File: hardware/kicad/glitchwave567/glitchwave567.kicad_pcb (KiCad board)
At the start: 2 copper layers, 0 parts

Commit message: hardware: LAYOUT phase 1 - both boards placed via pcbnew API (296+22 footprints, nets bound)
pcbgen.py: netlist-driven board authoring (pcbnew python 7.0.11) - footprint
instantiation with per-pad net binding, corner-notched outline, spiral
auto-placement of passives near net-neighbor anchors (pad-extent collision),
GND zones both layers staged. Wall jacks auto-oriented; audit confirms zero
pads outside outline. Audio chain right-to-left (IN->dirt->567->SVF->OUT),
buck top-center, Pico+digital bottom, ctrl board pots 3+3 grid at drill
positions, header at identical enclosure XY on both boards (stack mates).
Routing (custom grid A*) next.

Co-Authored-By: Claude Fable 5 <noreply@anthropic.com>
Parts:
- added C1: 220n, C_0603_1608Metric, F.Cu at (126.4, 42.0)
- added C100: 220u/35V, CP_Elec_8x10, F.Cu at (70.8, 25.0)
- added C101: 100n, C_0603_1608Metric, F.Cu at (70.0, 28.2)
- added C102: 1u, C_0603_1608Metric, F.Cu at (70.0, 21.8)
- added C103: 1u, C_0603_1608Metric, F.Cu at (73.8, 27.9)
- added C104: 10u/50V X7R, C_1206_3216Metric, F.Cu at (72.0, 31.1)
- added C105: 3n3, C_0603_1608Metric, F.Cu at (73.8, 22.1)
- added C106: 100n, C_0603_1608Metric, F.Cu at (88.0, 20.0)
- added C107: 100n, C_0603_1608Metric, F.Cu at (66.3, 29.2)
- added C108: 22u, C_0805_2012Metric, F.Cu at (64.8, 21.2)
- added C109: 47u, CP_Elec_6.3x5.4, F.Cu at (53.8, 36.3)
- added C110: 47u, CP_Elec_6.3x5.4, F.Cu at (68.4, 18.0)
- added C111: 100n, C_0603_1608Metric, F.Cu at (63.0, 26.6)
- added C120: 1n, C_0603_1608Metric, F.Cu at (48.7, 109.5)
- added C121: 100n, C_0603_1608Metric, F.Cu at (75.7, 19.3)
- added C122: 100n, C_0603_1608Metric, F.Cu at (76.6, 30.8)
- added C123: 100n, C_0603_1608Metric, F.Cu at (97.6, 106.8)
- added C124: 100n, C_0603_1608Metric, F.Cu at (93.2, 106.8)
- added C2: 4.7u, CP_Elec_4x5.4, F.Cu at (75.0, 34.1)
- added C20: 100n, C_0603_1608Metric, F.Cu at (122.0, 48.1)
- added C21: 100n, C_0603_1608Metric, F.Cu at (122.4, 50.5)
- added C22: 100n, C_0603_1608Metric, F.Cu at (117.3, 47.8)
- added C23: 100n, C_0603_1608Metric, F.Cu at (117.7, 50.2)
- added C3: 220n, C_0603_1608Metric, F.Cu at (114.0, 44.4)
- added C30: 100n, C_0603_1608Metric, F.Cu at (128.0, 79.2)
- added C31: 100n, C_0603_1608Metric, F.Cu at (128.0, 72.8)
- added C32: 3.9n, C_0603_1608Metric, F.Cu at (62.1, 28.8)
- added C33: 100n, C_0603_1608Metric, F.Cu at (61.2, 24.2)
- added C34: 100n, C_0603_1608Metric, F.Cu at (78.2, 21.9)
- added C35: 100n, C_0603_1608Metric, F.Cu at (60.9, 21.9)
- added C40: 100n, C_0603_1608Metric, F.Cu at (69.2, 15.4)
- added C41: DNP-LFIL, C_0603_1608Metric, F.Cu at (97.0, 54.0)
- added C42: DNP-OFIL, C_0603_1608Metric, F.Cu at (97.0, 46.0)
- added C43: 220p, C_0603_1608Metric, F.Cu at (73.5, 15.2)
- added C44: 1u, C_0603_1608Metric, F.Cu at (77.3, 16.5)
- added C45: 47n, C_0603_1608Metric, F.Cu at (103.4, 82.0)
- added C46: 1u, C_0603_1608Metric, F.Cu at (91.0, 84.4)
- added C47: 22u, CP_Elec_5x5.4, F.Cu at (98.6, 89.0)
- added C48: 470u, CP_Elec_10x10, F.Cu at (97.0, 74.8)
- added C49: 100n, C_0603_1608Metric, F.Cu at (79.4, 18.9)
- added C50: 100n, C_0603_1608Metric, F.Cu at (82.0, 25.0)
- added C60: 220n, C_0603_1608Metric, F.Cu at (73.9, 12.8)
- added C61: 220p, C_0603_1608Metric, F.Cu at (68.4, 52.0)
- added C62: 220p, C_0603_1608Metric, F.Cu at (56.0, 54.4)
- added C63: 100n, C_0603_1608Metric, F.Cu at (81.6, 28.1)
- added C64: 100n, C_0603_1608Metric, F.Cu at (80.4, 31.0)
- added C65: 100n, C_0603_1608Metric, F.Cu at (71.6, 36.9)
- added C66: 100n, C_0603_1608Metric, F.Cu at (57.2, 24.2)
- added C67: 100n, C_0603_1608Metric, F.Cu at (82.4, 21.9)
- added C70: 100n, C_0603_1608Metric, F.Cu at (76.8, 36.8)
- added C71: 100n, C_0603_1608Metric, F.Cu at (77.2, 39.1)
- added C72: 47n, C_0603_1608Metric, F.Cu at (56.8, 21.9)
- added C72A: 56n, C_0603_1608Metric, F.Cu at (44.4, 44.0)
- added C73: 100n, C_0603_1608Metric, F.Cu at (19.5, 79.7)
- added C74: 1u, C_0603_1608Metric, F.Cu at (27.5, 79.7)
- added C75: 10u, CP_Elec_4x5.4, F.Cu at (24.4, 58.4)
- added C76: 100n, C_0603_1608Metric, F.Cu at (57.8, 18.9)
- added C77: 100n, C_0603_1608Metric, F.Cu at (78.1, 14.1)
- added C78: 100n, C_0603_1608Metric, F.Cu at (81.4, 33.8)
- added C8: 220n, C_0603_1608Metric, F.Cu at (80.8, 36.8)
- added C80: 1u, C_0603_1608Metric, F.Cu at (91.0, 101.4)
- added C81: 10n, C_0603_1608Metric, F.Cu at (44.0, 109.6)
- added C82: 10n, C_0603_1608Metric, F.Cu at (42.5, 84.7)
- added C83: 100n, C_0603_1608Metric, F.Cu at (72.0, 39.3)
- added C84: 100n, C_0603_1608Metric, F.Cu at (90.7, 98.2)
- added C85: 100n, C_0603_1608Metric, F.Cu at (67.2, 39.1)
- added C90: 10u, CP_Elec_4x5.4, F.Cu at (48.7, 84.5)
- added C91: 100n, C_0603_1608Metric, F.Cu at (57.7, 16.1)
- added C910: 100n, C_0603_1608Metric, F.Cu at (73.2, 10.1)
- added C911: 100n, C_0603_1608Metric, F.Cu at (49.0, 32.4)
- added C93: 100n, C_0603_1608Metric, F.Cu at (77.6, 11.8)
- added C94: 100n, C_0603_1608Metric, F.Cu at (86.0, 25.0)
- added C95: 100n, C_0603_1608Metric, F.Cu at (62.5, 39.1)
- added C96: 100n, C_0603_1608Metric, F.Cu at (68.0, 41.7)
- added C97: 100n, C_0603_1608Metric, F.Cu at (53.2, 24.2)
- added C98: 100n, C_0603_1608Metric, F.Cu at (73.9, 7.84)
- added C99: 100n, C_0603_1608Metric, F.Cu at (78.3, 9.50)
- added D1: 1N4148W, D_SOD-123, F.Cu at (128.4, 81.6)
- added D100: BZT52C10, D_SOD-123, F.Cu at (53.5, 8.30)
- added D101: SS34, D_SMA, F.Cu at (94.0, 26.0)
- added D102: 1N4148W, D_SOD-123, F.Cu at (62.4, 41.8)
- added D103: BZT52C6V2, D_SOD-123, F.Cu at (86.1, 35.5)
- added D104: 1N4148W, D_SOD-123, F.Cu at (87.7, 38.3)
- added D105: 1N4148W (drop: LM567C abs max 9V vs 78L09 +5% tol), D_SOD-123, F.Cu at (87.0, 31.0)
- added D106: SMAJ18A (VA transient clamp), D_SMA, F.Cu at (50.0, 20.0)
- added D70: 1N4148W, D_SOD-123, F.Cu at (40.0, 50.1)
- added D71: 1N4148W, D_SOD-123, F.Cu at (36.8, 37.7)
- added D72: 1N4148W, D_SOD-123, F.Cu at (35.2, 34.9)
- added D73: 1N4148W, D_SOD-123, F.Cu at (31.0, 45.6)
- added D74: 1N4148W, D_SOD-123, F.Cu at (31.0, 42.4)
- added D75: 1N4148W, D_SOD-123, F.Cu at (29.4, 39.6)
- added D80: 1N4148W, D_SOD-123, F.Cu at (95.8, 92.7)
- added D81: 1N4148W, D_SOD-123, F.Cu at (104.0, 97.4)
- added D82: 1N4148W, D_SOD-123, F.Cu at (101.4, 92.3)
- added D83: 1N5819W (clamp 3V3), D_SOD-123, F.Cu at (81.8, 40.2)
- added D84: 1N5819W, D_SOD-123, F.Cu at (57.0, 39.1)
- added D85: 1N5819W, D_SOD-123, F.Cu at (52.4, 17.3)
- added D90: SS14 (+5V->VSYS), D_SMA, F.Cu at (54.9, 110.3)
- added FB100: 600R/3A, L_1206_3216Metric, F.Cu at (61.0, 16.0)
- added J1: IN 6.35mm PJ-603A, PJ-603A, F.Cu at (110.0, 0.80)
- added J10: CTRL 2x8, PinHeader_2x08_P2.54mm_Vertical, F.Cu at (96.0, 104.0)
- added J2: OUT 6.35mm PJ-603A, PJ-603A, F.Cu at (28.0, 0.80)
- added J3: CV1 IN 3.5mm PJ-3410, PJ-3410, F.Cu at (0.80, 40.0)
- added J4: CV2 IN 3.5mm PJ-3410, PJ-3410, F.Cu at (0.80, 75.0)
- added J5: DC_2.1mm, DC-044A, F.Cu at (69.0, 2.00)
- added J6: CV OUT 3.5mm PJ-3410, PJ-3410, F.Cu at (137.2, 57.0)
- added L100: 22uH/3A SMDRI127, L_12x12mm_H8mm, F.Cu at (101.0, 22.0)
- added Q1: MMBTA13, SOT-23, F.Cu at (128.0, 76.0)
- added Q10: AO3401A, SOT-23, F.Cu at (55.0, 12.0)
- added Q11: BCP56, SOT-223-3_TabPin2, F.Cu at (64.0, 34.0)
- added Q2: MMBT3904, SOT-23, F.Cu at (90.7, 81.2)
- added Q3: MMBT3904, SOT-23, F.Cu at (103.5, 85.1)
- added Q4: MMBT3904, SOT-23, F.Cu at (80.4, 74.0)
- added Q5: MMBT3904, SOT-23, F.Cu at (67.7, 74.8)
- added Q6: MMBT3904, SOT-23, F.Cu at (74.0, 81.2)
- added QJ1: MMBFJ201, SOT-23, F.Cu at (27.5, 82.9)
- added R1: 1k, R_0603_1608Metric, F.Cu at (126.8, 44.4)
- added R100: 100k, R_0603_1608Metric, F.Cu at (53.9, 5.94)
- added R100A: 39k, R_0603_1608Metric, F.Cu at (79.9, 43.3)
- added R101: 100k, R_0603_1608Metric, F.Cu at (88.0, 12.0)
- added R101A: 18k, R_0603_1608Metric, F.Cu at (35.3, 49.8)
- added R102: 51k, R_0603_1608Metric, F.Cu at (91.7, 20.2)
- added R102A: 3.6k, R_0603_1608Metric, F.Cu at (44.5, 47.1)
- added R103: 100k, R_0603_1608Metric, F.Cu at (84.3, 11.8)
- added R103A: 4.3k, R_0603_1608Metric, F.Cu at (44.5, 40.9)
- added R104: 40k2 1%, R_0603_1608Metric, F.Cu at (91.7, 11.8)
- added R105: 7k68 1%, R_0603_1608Metric, F.Cu at (92.1, 9.40)
- added R106: 47k, R_0603_1608Metric, F.Cu at (48.7, 29.2)
- added R106A: 10k, R_0603_1608Metric, F.Cu at (18.0, 72.0)
- added R107: 47k, R_0603_1608Metric, F.Cu at (48.5, 26.9)
- added R107A: 10k, R_0603_1608Metric, F.Cu at (18.4, 69.6)
- added R108: 33k, R_0603_1608Metric, F.Cu at (48.9, 23.6)
- added R108A: 1M, R_0603_1608Metric, F.Cu at (19.9, 82.1)
- added R109: 147k, R_0603_1608Metric, F.Cu at (44.9, 23.6)
- added R109A: 845R 1% (Fetzer Rs), R_0603_1608Metric, F.Cu at (32.3, 82.9)
- added R110: 10k, R_0603_1608Metric, F.Cu at (90.9, 35.5)
- added R110A: 15k, R_0603_1608Metric, F.Cu at (31.5, 79.7)
- added R111: 10k, R_0603_1608Metric, F.Cu at (88.1, 40.6)
- added R111A: 220k, R_0603_1608Metric, F.Cu at (26.0, 72.0)
- added R112: 100k, R_0603_1608Metric, F.Cu at (86.8, 96.0)
- added R112A: 10k, R_0603_1608Metric, F.Cu at (31.3, 48.4)
- added R113: 22k, R_0603_1608Metric, F.Cu at (86.2, 99.1)
- added R113A: 10k, R_0603_1608Metric, F.Cu at (42.4, 37.3)
- added R114: 24k9 (EN divider - EN abs max 6V!), R_0603_1608Metric, F.Cu at (94.4, 16.0)
- added R114A: 3.3k, R_0603_1608Metric, F.Cu at (44.6, 49.8)
- added R115A: 6.8k, R_0603_1608Metric, F.Cu at (40.7, 52.4)
- added R116A: 4.7k, R_0603_1608Metric, F.Cu at (36.0, 52.6)
- added R117A: 10k, R_0603_1608Metric, F.Cu at (31.5, 51.1)
- added R118A: 220k, R_0603_1608Metric, F.Cu at (44.4, 60.0)
- added R119A: 680, R_0603_1608Metric, F.Cu at (32.0, 62.4)
- added R12: 100k, R_0603_1608Metric, F.Cu at (84.4, 42.7)
- added R120A: 680, R_0603_1608Metric, F.Cu at (31.7, 59.2)
- added R121A: 10k, R_0603_1608Metric, F.Cu at (44.5, 63.1)
- added R122A: 220k, R_0603_1608Metric, F.Cu at (41.1, 66.5)
- added R123A: 680, R_0603_1608Metric, F.Cu at (36.4, 67.0)
- added R124A: 680, R_0603_1608Metric, F.Cu at (31.5, 56.9)
- added R125A: 10k, R_0603_1608Metric, F.Cu at (44.5, 56.9)
- added R126A: 220k, R_0603_1608Metric, F.Cu at (31.9, 66.4)
- added R127A: 100k, R_0603_1608Metric, F.Cu at (26.0, 61.2)
- added R13: 470R, R_0603_1608Metric, F.Cu at (21.6, 61.2)
- added R130: 100k, R_0603_1608Metric, F.Cu at (90.5, 95.9)
- added R131: 100k, R_0603_1608Metric, F.Cu at (89.9, 104.2)
- added R132: 100k, R_0603_1608Metric, F.Cu at (91.1, 93.5)
- added R133: 200k, R_0603_1608Metric, F.Cu at (102.3, 107.0)
- added R134: 100k, R_0603_1608Metric, F.Cu at (99.0, 109.2)
- added R135: 3.9k, R_0603_1608Metric, F.Cu at (103.0, 95.1)
- added R136: 150k, R_0603_1608Metric, F.Cu at (107.0, 95.1)
- added R137: 100k, R_0603_1608Metric, F.Cu at (94.2, 109.0)
- added R138: 47k, R_0603_1608Metric, F.Cu at (90.5, 110.6)
- added R139: 1k, R_0603_1608Metric, F.Cu at (89.5, 108.2)
- added R140: 100k, R_0603_1608Metric, F.Cu at (57.4, 41.5)
- added R141: 47k, R_0603_1608Metric, F.Cu at (56.6, 43.9)
- added R142: 10k, R_0603_1608Metric, F.Cu at (52.8, 41.4)
- added R143: 100k, R_0603_1608Metric, F.Cu at (52.8, 14.9)
- added R144: 47k, R_0603_1608Metric, F.Cu at (47.7, 16.5)
- added R145: 10k, R_0603_1608Metric, F.Cu at (49.2, 13.8)
- added R146: 10k, R_0603_1608Metric, F.Cu at (67.9, 44.2)
- added R147: 10k, R_0603_1608Metric, F.Cu at (68.1, 48.1)
- added R148: 10k, R_0603_1608Metric, F.Cu at (86.9, 101.4)
- added R149: 20k, R_0603_1608Metric, F.Cu at (90.1, 91.2)
- added R150: 1k, R_0603_1608Metric, F.Cu at (92.3, 88.8)
- added R16: 100k, R_0603_1608Metric, F.Cu at (73.9, 5.65)
- added R161: 10k, R_0603_1608Metric, F.Cu at (78.8, 7.18)
- added R162: 10k, R_0603_1608Metric, F.Cu at (40.2, 110.2)
- added R163: 10k, R_0603_1608Metric, F.Cu at (38.8, 84.5)
- added R164: 10k, R_0603_1608Metric, F.Cu at (42.8, 82.1)
- added R165: 10k, R_0603_1608Metric, F.Cu at (47.6, 81.9)
- added R166: 10k, R_0603_1608Metric, F.Cu at (54.9, 84.7)
- added R167: 10k, R_0603_1608Metric, F.Cu at (35.8, 109.4)
- added R168: 10k, R_0603_1608Metric, F.Cu at (38.1, 82.2)
- added R169: 10k, R_0603_1608Metric, F.Cu at (51.8, 81.2)
- added R170: 1k, R_0603_1608Metric, F.Cu at (60.7, 109.5)
- added R171: 10k, R_0603_1608Metric, F.Cu at (103.6, 109.9)
- added R172: 10k, R_0603_1608Metric, F.Cu at (105.9, 107.1)
- added R173: 100R, R_0603_1608Metric, F.Cu at (66.0, 111.2)
- added R174: 10k, R_0603_1608Metric, F.Cu at (83.2, 8.75)
- added R2: 2.2M, R_0603_1608Metric, F.Cu at (126.8, 39.6)
- added R20: 43k, R_0603_1608Metric, F.Cu at (126.0, 48.1)
- added R21: 36k, R_0603_1608Metric, F.Cu at (113.7, 41.2)
- added R22: 100k, R_0603_1608Metric, F.Cu at (113.6, 49.3)
- added R23: 15k, R_0603_1608Metric, F.Cu at (117.3, 36.2)
- added R24: 47k, R_0603_1608Metric, F.Cu at (126.4, 62.0)
- added R25: 10k, R_0603_1608Metric, F.Cu at (122.0, 68.1)
- added R3: 2.2M, R_0603_1608Metric, F.Cu at (122.0, 35.9)
- added R30: 220k, R_0603_1608Metric, F.Cu at (114.4, 70.0)
- added R31: 680, R_0603_1608Metric, F.Cu at (114.5, 73.1)
- added R32: 680, R_0603_1608Metric, F.Cu at (111.1, 76.5)
- added R33: 10k, R_0603_1608Metric, F.Cu at (106.4, 77.0)
- added R34: 330k, R_0603_1608Metric, F.Cu at (132.0, 79.2)
- added R35: 10k, R_0603_1608Metric, F.Cu at (128.4, 70.4)
- added R36: 4.7k, R_0603_1608Metric, F.Cu at (132.0, 72.8)
- added R37: 1M, R_0603_1608Metric, F.Cu at (132.4, 75.2)
- added R38: 100k, R_0603_1608Metric, F.Cu at (100.7, 54.2)
- added R4: 470k, R_0603_1608Metric, F.Cu at (113.5, 38.9)
- added R40: 0R, R_0603_1608Metric, F.Cu at (93.3, 54.2)
- added R41: 100k, R_0603_1608Metric, F.Cu at (86.2, 92.9)
- added R42: 47k, R_0603_1608Metric, F.Cu at (80.4, 105.3)
- added R43: 47k, R_0603_1608Metric, F.Cu at (81.3, 16.5)
- added R44: 47k, R_0603_1608Metric, F.Cu at (86.8, 22.6)
- added R45: 220k, R_0603_1608Metric, F.Cu at (91.0, 68.4)
- added R46: 680, R_0603_1608Metric, F.Cu at (90.7, 65.2)
- added R47: 680, R_0603_1608Metric, F.Cu at (90.5, 62.9)
- added R48: 10k, R_0603_1608Metric, F.Cu at (93.9, 59.5)
- added R49: 10k, R_0603_1608Metric, F.Cu at (90.7, 78.0)
- added R5: 2.2k, R_0603_1608Metric, F.Cu at (116.5, 33.9)
- added R50: 47k, R_0603_1608Metric, F.Cu at (88.6, 86.6)
- added R51: 10k, R_0603_1608Metric, F.Cu at (105.0, 88.8)
- added R52: 47k, R_0603_1608Metric, F.Cu at (107.4, 82.0)
- added R53: 1k (pin3 clamp-current limit), R_0603_1608Metric, F.Cu at (93.3, 45.8)
- added R60: 1M, R_0603_1608Metric, F.Cu at (65.4, 15.2)
- added R61: 470k, R_0603_1608Metric, F.Cu at (73.1, 3.28)
- added R62: 680, R_0603_1608Metric, F.Cu at (80.4, 60.0)
- added R63: 680, R_0603_1608Metric, F.Cu at (68.0, 62.4)
- added R64: 10k, R_0603_1608Metric, F.Cu at (67.7, 59.2)
- added R65: 220k, R_0603_1608Metric, F.Cu at (80.5, 63.1)
- added R66: 680, R_0603_1608Metric, F.Cu at (77.1, 66.5)
- added R67: 680, R_0603_1608Metric, F.Cu at (72.4, 67.0)
- added R68: 10k, R_0603_1608Metric, F.Cu at (72.4, 53.0)
- added R69: 220k, R_0603_1608Metric, F.Cu at (68.0, 71.6)
- added R70: 100k, R_0603_1608Metric, F.Cu at (80.5, 77.1)
- added R71: 100k, R_0603_1608Metric, F.Cu at (80.5, 70.9)
- added R72: 100k, R_0603_1608Metric, F.Cu at (80.4, 46.0)
- added R73: 100k, R_0603_1608Metric, F.Cu at (78.4, 80.7)
- added R74: 220k, R_0603_1608Metric, F.Cu at (55.7, 51.2)
- added R75: 680, R_0603_1608Metric, F.Cu at (63.6, 59.0)
- added R76: 10k, R_0603_1608Metric, F.Cu at (58.9, 58.5)
- added R77: 220k, R_0603_1608Metric, F.Cu at (55.5, 48.9)
- added R78: 680, R_0603_1608Metric, F.Cu at (60.4, 45.0)
- added R79: 10k, R_0603_1608Metric, F.Cu at (54.9, 57.2)
- added R80: 220k, R_0603_1608Metric, F.Cu at (56.0, 68.4)
- added R81: 680, R_0603_1608Metric, F.Cu at (55.7, 65.2)
- added R82: 680, R_0603_1608Metric, F.Cu at (62.0, 73.2)
- added R83: 10k, R_0603_1608Metric, F.Cu at (55.5, 62.9)
- added R84: 100k, R_0603_1608Metric, F.Cu at (80.5, 49.1)
- added R85: 100k, R_0603_1608Metric, F.Cu at (77.1, 52.5)
- added R86: 100k, R_0603_1608Metric, F.Cu at (81.6, 51.9)
- added R87: 51k, R_0603_1608Metric, F.Cu at (84.4, 46.0)
- added R88: 10k, R_0603_1608Metric, F.Cu at (85.2, 74.0)
- added R89: 47k, R_0603_1608Metric, F.Cu at (84.2, 76.9)
- added R90: 10k, R_0603_1608Metric, F.Cu at (67.7, 78.0)
- added R91: 47k, R_0603_1608Metric, F.Cu at (69.6, 80.7)
- added R92: 10k, R_0603_1608Metric, F.Cu at (74.0, 84.4)
- added R93: 47k, R_0603_1608Metric, F.Cu at (67.9, 67.6)
- added R94: 220k, R_0603_1608Metric, F.Cu at (54.4, 46.1)
- added R95: 680, R_0603_1608Metric, F.Cu at (55.1, 59.8)
- added R96: 220k, R_0603_1608Metric, F.Cu at (51.9, 54.4)
- added R97: 680, R_0603_1608Metric, F.Cu at (51.6, 51.2)
- added R98: 10k (buffer DC load), R_0603_1608Metric, F.Cu at (81.6, 68.1)
- added R99: 10k (buffer DC load), R_0603_1608Metric, F.Cu at (82.5, 80.0)
- added RV1: 10k trim (3224W), Potentiometer_Bourns_3224W_Vertical, F.Cu at (116.0, 96.0)
- added RV2: 10k trim (3224W), Potentiometer_Bourns_3224W_Vertical, F.Cu at (124.0, 96.0)
- added RV3: 10k trim (3224W), Potentiometer_Bourns_3224W_Vertical, F.Cu at (132.0, 96.0)
- added SW1: +6dB (short=OFF), SW_SPDT_PCM12, F.Cu at (18.0, 76.0)
- added SW2: JFET in/out, SW_SPDT_PCM12, F.Cu at (26.0, 76.0)
- added SW3: ladder in/out, SW_SPDT_PCM12, F.Cu at (34.0, 76.0)
- added U1: TL074, SOIC-14_3.9x8.7mm_P1.27mm, F.Cu at (120.0, 42.0)
- added U10: LM13700, SOIC-16_3.9x9.9mm_P1.27mm, F.Cu at (74.0, 60.0)
- added U11: LM13700, SOIC-16_3.9x9.9mm_P1.27mm, F.Cu at (62.0, 52.0)
- added U12: LM13700, SOIC-16_3.9x9.9mm_P1.27mm, F.Cu at (62.0, 66.0)
- added U13: CD4051B, SOIC-16_3.9x9.9mm_P1.27mm, F.Cu at (74.0, 74.0)
- added U14: TL074, SOIC-14_3.9x8.7mm_P1.27mm, F.Cu at (38.0, 44.0)
- added U15: LM13700, SOIC-16_3.9x9.9mm_P1.27mm, F.Cu at (38.0, 60.0)
- added U16: TL074, SOIC-14_3.9x8.7mm_P1.27mm, F.Cu at (24.0, 52.0)
- added U17: TL074, SOIC-14_3.9x8.7mm_P1.27mm, F.Cu at (97.0, 99.0)
- added U18: L78L09, SOT-89-3, F.Cu at (80.0, 27.0)
- added U19: MP1584EN, SOIC-8-1EP_3.9x4.9mm_P1.27mm_EP2.29x3mm, F.Cu at (88.0, 16.0)
- added U2: TL074, SOIC-14_3.9x8.7mm_P1.27mm, F.Cu at (120.0, 62.0)
- added U20: Raspberry Pi Pico, RPi_Pico_SMD, F.Cu at (46.0, 97.0)
- added U21: 74HC4067, SOIC-24W_7.5x15.4mm_P1.27mm, F.Cu at (78.0, 96.0)
- added U22: 74AHCT1G125, SOT-23-5, F.Cu at (66.0, 108.0)
- added U3: LM13700, SOIC-16_3.9x9.9mm_P1.27mm, F.Cu at (108.0, 70.0)
- added U5: LM567 (SO-8), SOIC-8_3.9x4.9mm_P1.27mm, F.Cu at (97.0, 50.0)
- added U6: TL074, SOIC-14_3.9x8.7mm_P1.27mm, F.Cu at (55.0, 30.0)
- added U7: LM13700, SOIC-16_3.9x9.9mm_P1.27mm, F.Cu at (97.0, 66.0)
- added U8: CD4052B, SOIC-16_3.9x9.9mm_P1.27mm, F.Cu at (97.0, 82.0)
- added U9: TL074, SOIC-14_3.9x8.7mm_P1.27mm, F.Cu at (74.0, 46.0)
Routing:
- added copper zone on B.Cu, net GND
- added copper zone on F.Cu, net GND
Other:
- board outline added: 138 x 114 mm
- board text added: "BACK WALL: OUT / DC 9-18V ctr-neg / IN"
- board text added: "GLITCHWAVE 567 - MAIN rev0.1 Illicit Apothecary"

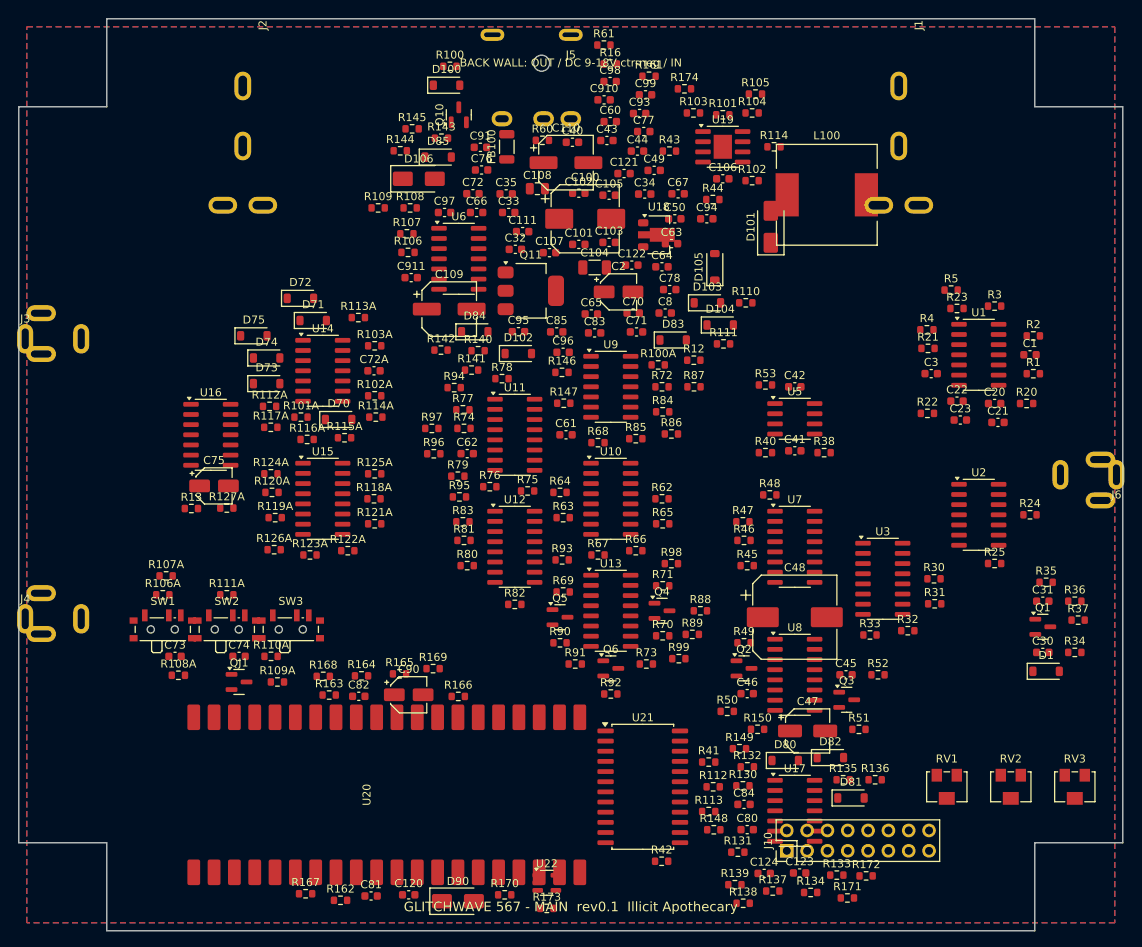
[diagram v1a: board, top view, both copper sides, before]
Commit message: hardware: ROUTING complete (0 unrouted nets both boards) via custom grid A* - DRC punch list captured
router.py: 0.508mm grid A*, F.Cu-horizontal/B.Cu-vertical bias, 45deg moves,
via cost, pad-escape cells, rotation-aware pad claims, same-net adjacent-pin
preroute w/ union-join, best-of-N orderings + priority retry. MAIN 210 nets
routed after placement fixes (env chain + U17 relocated from walled pocket);
CTRL 16 nets. GND pours filled + stitching vias.
KNOWN DRC punch list (KiCad 10): diagonal track crossings (need corner-cut
rule), preroute segments crossing intermediate pads (need corridor check),
hole clearance margin, starved thermals -> solid pad connection, 98
unconnected (drc_main.json has items). Fix round next.

Co-Authored-By: Claude Fable 5 <noreply@anthropic.com>
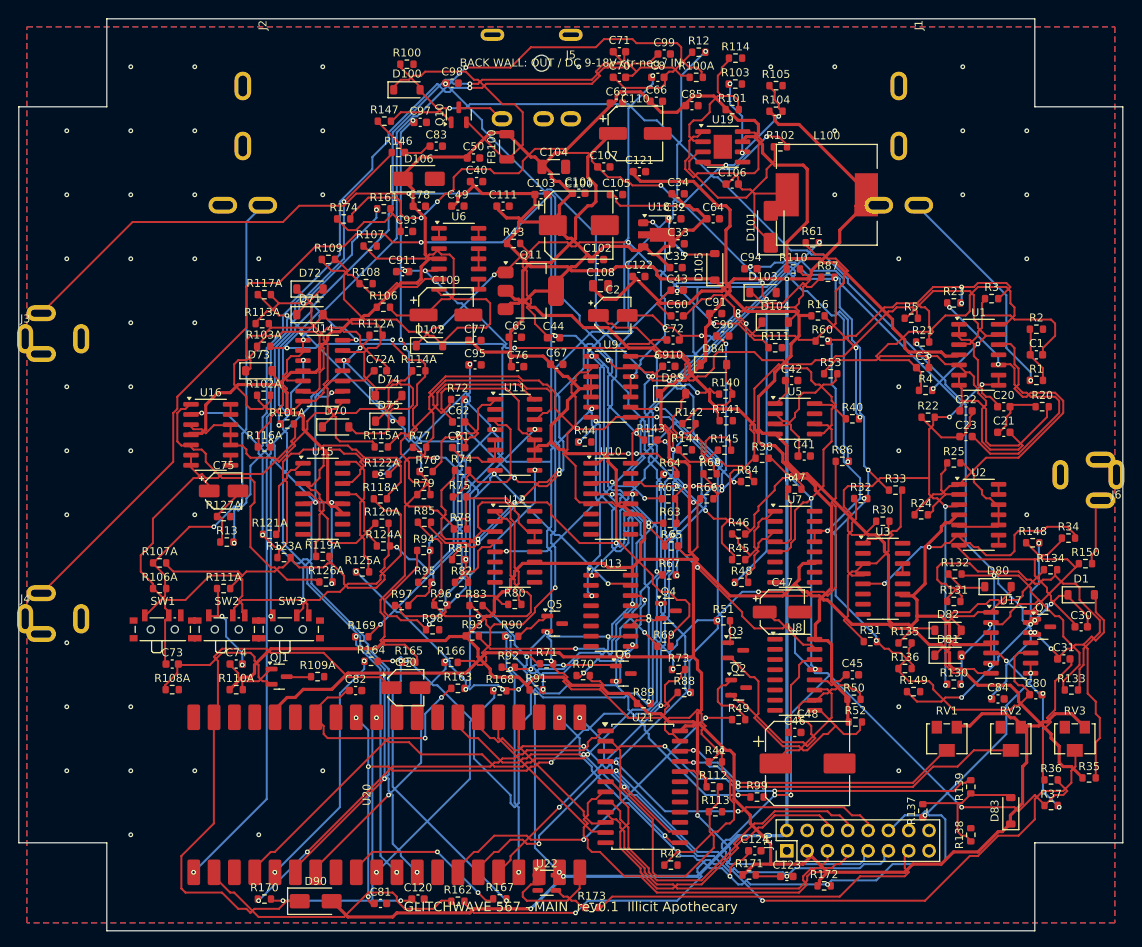
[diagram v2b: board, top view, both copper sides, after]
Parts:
- moved D83 72.4 mm to (124.0, 99.0), turned to 90 degrees
- moved R145 56.0 mm to (88.2, 53.9)
- moved R148 53.6 mm to (126.7, 65.5)
- moved R144 51.6 mm to (83.3, 53.9)
- moved R134 50.3 mm to (129.0, 68.9)
- moved R150 45.9 mm to (133.3, 68.1)
- moved R143 45.9 mm to (79.0, 52.7)
- moved R174 45.6 mm to (40.6, 25.0)
- moved R60 43.0 mm to (100.4, 40.3)
- moved R147 41.8 mm to (45.7, 12.8)
- moved D85 41.6 mm to (81.7, 46.9)
- moved R131 41.4 mm to (116.9, 72.8)
- moved R16 40.8 mm to (99.9, 37.1)
- moved C80 39.8 mm to (127.1, 84.5)
- moved R12 38.5 mm to (85.0, 4.18)
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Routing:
- net VA: track 0.00 -> 490.5 mm
- net VREF: track 0.00 -> 401.8 mm, vias 0 -> 25
- net 3V3: track 0.00 -> 239.3 mm
- net +5V: track 0.00 -> 194.6 mm, vias 0 -> 3
- net DRY_CLEAN: track 0.00 -> 182.7 mm, vias 0 -> 7
- net GATE_VOL_CV: track 0.00 -> 157.3 mm, vias 0 -> 4
- net DIRT_CV: track 0.00 -> 138.5 mm, vias 0 -> 5
- net VDIRT: track 0.00 -> 136.9 mm
- net DIRT_OUT: track 0.00 -> 133.1 mm, vias 0 -> 6
- net /env_cv/CVF2: track 0.00 -> 130.7 mm, vias 0 -> 3
- net CV2_TIP: track 0.00 -> 128.7 mm, vias 0 -> 2
- net V567: track 0.00 -> 124.1 mm
- net /mix_svf/SVF_HP: track 0.00 -> 123.6 mm, vias 0 -> 7
- net Q_OUT: track 0.00 -> 115.2 mm, vias 0 -> 4
- net MIX_DRY_CV: track 0.00 -> 113.2 mm, vias 0 -> 4
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
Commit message: hardware: router physics tuned (grid 0.55 + diagonals + pad-graze guard + 0.13mm design rules); ctrl 100% routed, main ~195/210; 3D renders
Co-Authored-By: Claude Fable 5 <noreply@anthropic.com>
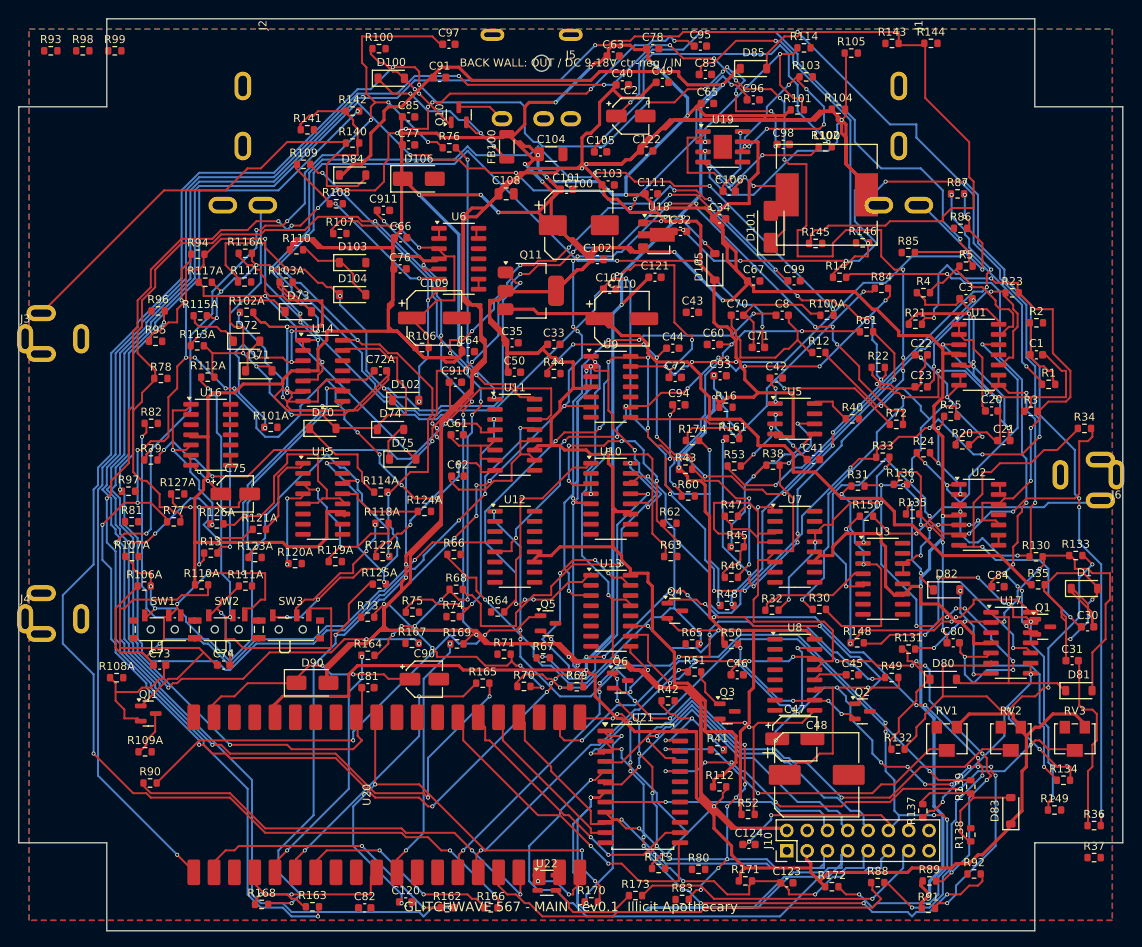
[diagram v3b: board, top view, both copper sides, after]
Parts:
- moved R99 123.1 mm to (12.0, 4.00)
- moved R93 90.1 mm to (4.00, 4.00)
- moved R98 84.6 mm to (8.00, 4.00)
- moved R85 69.2 mm to (111.2, 29.2)
- moved R111 66.8 mm to (28.2, 32.9)
- moved R141 63.8 mm to (36.1, 13.9)
- moved R92 63.7 mm to (119.4, 106.9)
- moved R110 62.2 mm to (34.7, 28.9)
- moved R147 60.2 mm to (102.6, 32.3)
- moved R144 59.4 mm to (114.0, 3.07)
- moved R146 59.1 mm to (105.5, 28.0)
- moved R143 58.0 mm to (109.2, 3.08)
- moved R142 57.4 mm to (41.7, 11.5)
- moved R140 56.2 mm to (41.7, 15.5)
- moved R91 56.1 mm to (113.7, 111.2)
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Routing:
- net VA: track 490.5 -> 732.6 mm, vias 0 -> 18
- net DIRT_CV: track 138.5 -> 357.0 mm, vias 5 -> 12
- net +5V: track 194.6 -> 402.8 mm, vias 3 -> 2
- net VREF: track 401.8 -> 197.3 mm
- net /mcu/PWM_FREQ: track 93.7 -> 290.9 mm, vias 2 -> 16
- net SVF_Q_CV: track 92.4 -> 239.3 mm, vias 2 -> 12
- net /mix_svf/SVF_BP: track 79.0 -> 219.9 mm, vias 5 -> 22
- net CV2_TIP: track 128.7 -> 0.00 mm, vias 2 -> 0
- net /mix_svf/FMODE_B_S: track 19.5 -> 143.2 mm, vias 3 -> 25
- net /mix_svf/SVF_HP: track 123.6 -> 0.00 mm, vias 7 -> 0
- net Q_OUT: track 115.2 -> 0.00 mm, vias 4 -> 0
- net SVF_F_CV: track 76.0 -> 181.3 mm, vias 4 -> 11
- net CVOUT_PWM: track 103.8 -> 0.00 mm, vias 2 -> 0
- net /mix_svf/SVF_LP: track 102.7 -> 0.00 mm, vias 5 -> 0
- net CV2_ADC: track 95.2 -> 0.00 mm, vias 2 -> 0
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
